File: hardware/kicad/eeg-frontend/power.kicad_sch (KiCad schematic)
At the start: 26 parts, among them Q1 DMP3099L, U3 LM2664M6/NOPB, U4 MCP1754T-3302E/OT, U5 TPS72325DBV, U6 TLV70025_SOT23-5

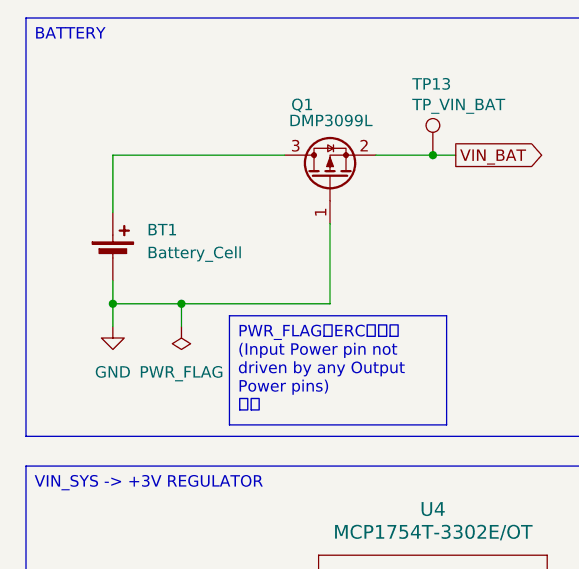
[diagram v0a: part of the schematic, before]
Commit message: Assign footprints to schematic components
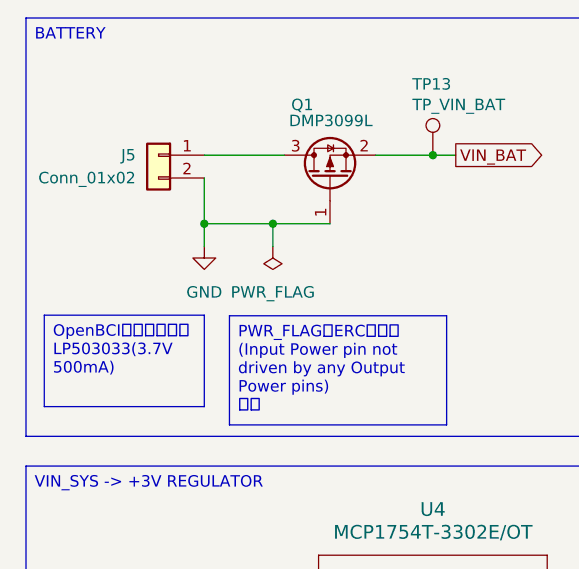
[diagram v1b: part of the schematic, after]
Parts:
- removed BT1: Battery_Cell, symbol Device:Battery_Cell
- added J5: Conn_01x02, Connector_JST:JST_PH_B2B-PH-K_1x02_P2.00mm_Vertical, symbol Connector_Generic:Conn_01x02
- C1, C10, C11, C2, C21, C5, C6, C7, C8, C9: footprint (none) -> Capacitor_SMD:C_0603_1608Metric_Pad1.08x0.95mm_HandSolder
- C20, C3, C4: footprint (none) -> Capacitor_SMD:C_0805_2012Metric_Pad1.18x1.45mm_HandSolder
- JP1: footprint (none) -> Connector_PinHeader_2.54mm:PinHeader_1x03_P2.54mm_Vertical
- TP10, TP11, TP13, TP7, TP8, TP9: footprint (none) -> TestPoint:TestPoint_Pad_D2.0mm
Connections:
- net GND: now also J5.2 (Pin_2)
- net at Q1.3 (D): now also J5.1 (Pin_1)

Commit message: 一旦できたと思ったPCB。 しかしPMODのコネクタの位置が左右で逆で、このまま刺すとGNDの一に通常のデータ信号的なのが来てしまう。
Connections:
- net GND renamed AGND
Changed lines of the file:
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@@
 			)
 		)
-		(property "Value" "GND"
-			(at 40.64 109.22 0)
-			(show_name no)
-			(do_not_autoplace no)
-			(effects
-				(font
-					(size 1.27 1.27)
-				)
+		(property "Value" "AGND"
+			(at 43.18 105.4099 0)
+			(show_name no)
+			(do_not_autoplace no)
+			(effects
+				(font
+					(size 1.27 1.27)
+				)
+				(justify left)
 			)
 		)
@@
 			)
 		)
-		(property "Value" "GND"
-			(at 118.11 58.42 0)
-			(show_name no)
-			(do_not_autoplace no)
-			(effects
-				(font
-					(size 1.27 1.27)
-				)
+		(property "Value" "AGND"
+			(at 120.65 54.6099 0)
+			(show_name no)
+			(do_not_autoplace no)
+			(effects
+				(font
+					(size 1.27 1.27)
+				)
+				(justify left)
 			)
 		)
@@
 			)
 		)
-		(property "Value" "GND"
-			(at 165.1 113.03 0)
-			(show_name no)
-			(do_not_autoplace no)
-			(effects
-				(font
-					(size 1.27 1.27)
-				)
+		(property "Value" "AGND"
+			(at 167.64 109.2199 0)
+			(show_name no)
+			(do_not_autoplace no)
+			(effects
+				(font
+					(size 1.27 1.27)
+				)
+				(justify left)
 			)
 		)
@@
 			)
 		)
-		(property "Value" "GND"
-			(at 64.77 158.75 0)
-			(show_name no)
-			(do_not_autoplace no)
-			(effects
-				(font
-					(size 1.27 1.27)
-				)
+		(property "Value" "AGND"
+			(at 67.31 154.9399 0)
+			(show_name no)
+			(do_not_autoplace no)
+			(effects
+				(font
+					(size 1.27 1.27)
+				)
+				(justify left)
 			)
 		)
@@
 			)
 		)
-		(property "Value" "GND"
-			(at 166.37 158.75 0)
-			(show_name no)
-			(do_not_autoplace no)
-			(effects
-				(font
-					(size 1.27 1.27)
-				)
+		(property "Value" "AGND"
+			(at 168.91 154.9399 0)
+			(show_name no)
+			(do_not_autoplace no)
+			(effects
+				(font
+					(size 1.27 1.27)
+				)
+				(justify left)
 			)
 		)
@@
 		(in_pos_files yes)
 		(dnp no)
-		(fields_autoplaced yes)
 		(property "Reference" "#PWR02"
 			(at 35.56 46.99 0)
@@
 			)
 		)
-		(property "Value" "GND"
-			(at 35.56 45.72 0)
-			(show_name no)
-			(do_not_autoplace no)
-			(effects
-				(font
-					(size 1.27 1.27)
-				)
-			)
-		)
+		(property "Value" "AGND"
+			(at 28.448 42.164 0)
+			(show_name no)
+			(do_not_autoplace no)
+			(effects
+				(font
+					(size 1.27 1.27)
+				)
+				(justify left)
+			)
+		)
